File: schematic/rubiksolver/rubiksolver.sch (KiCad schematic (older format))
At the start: 14 parts, among them M1 Stepper_Motor_bipolar, M2 Stepper_Motor_bipolar, M3 Stepper_Motor_bipolar, M4 Stepper_Motor_bipolar

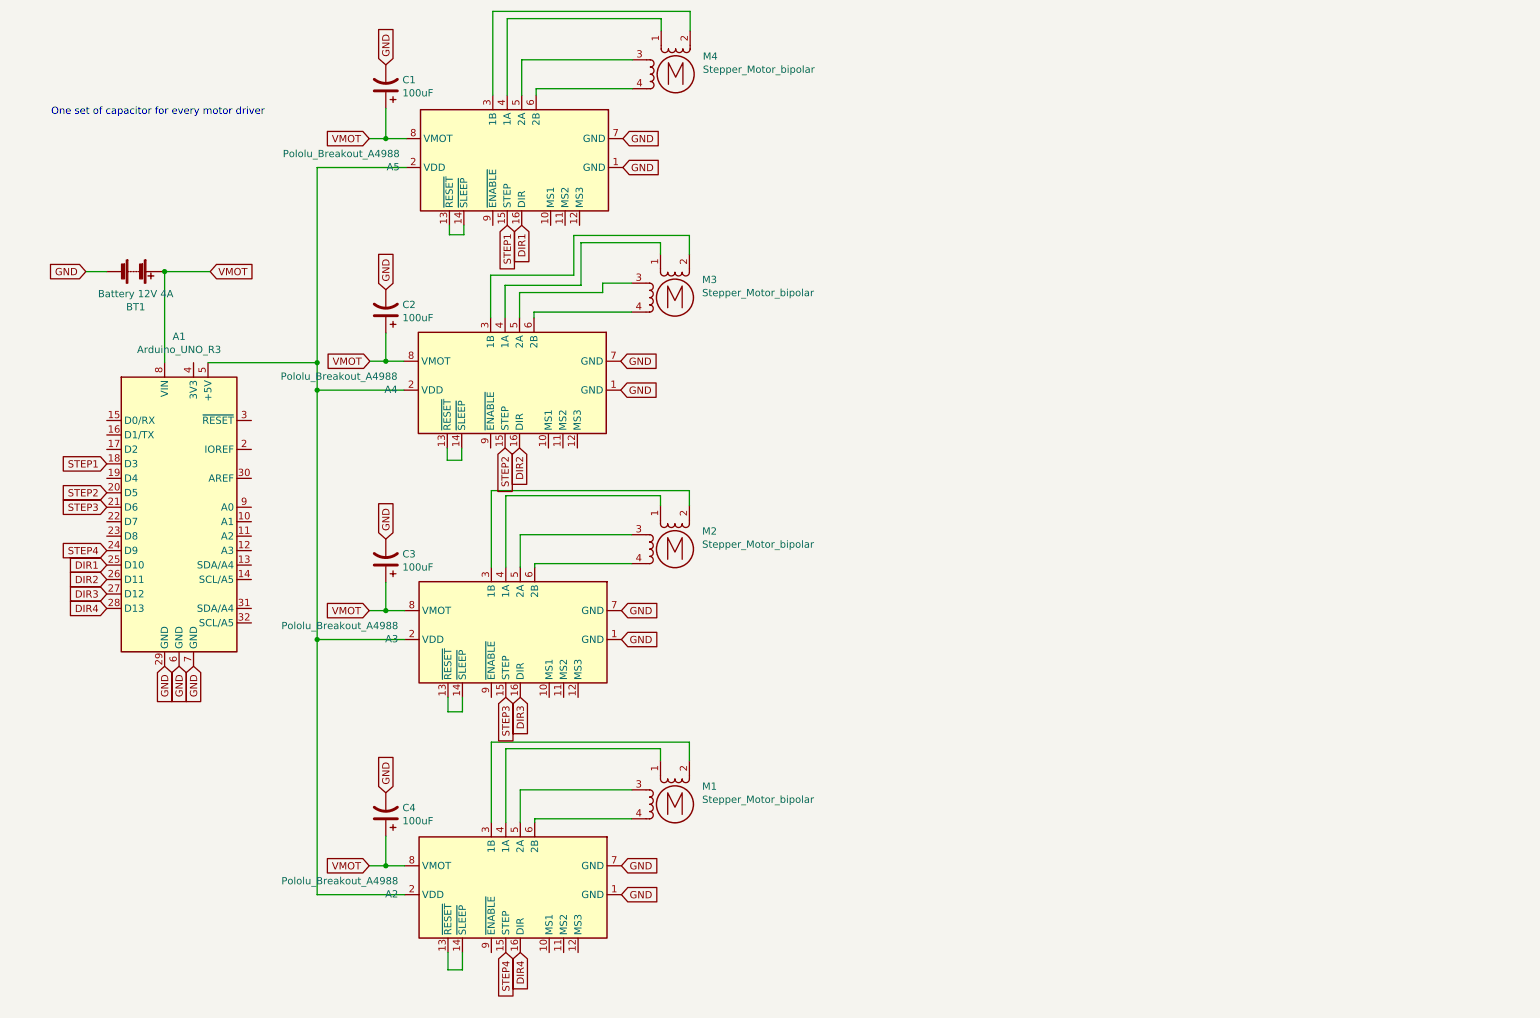
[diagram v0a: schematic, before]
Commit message: Changed models; updated schematic
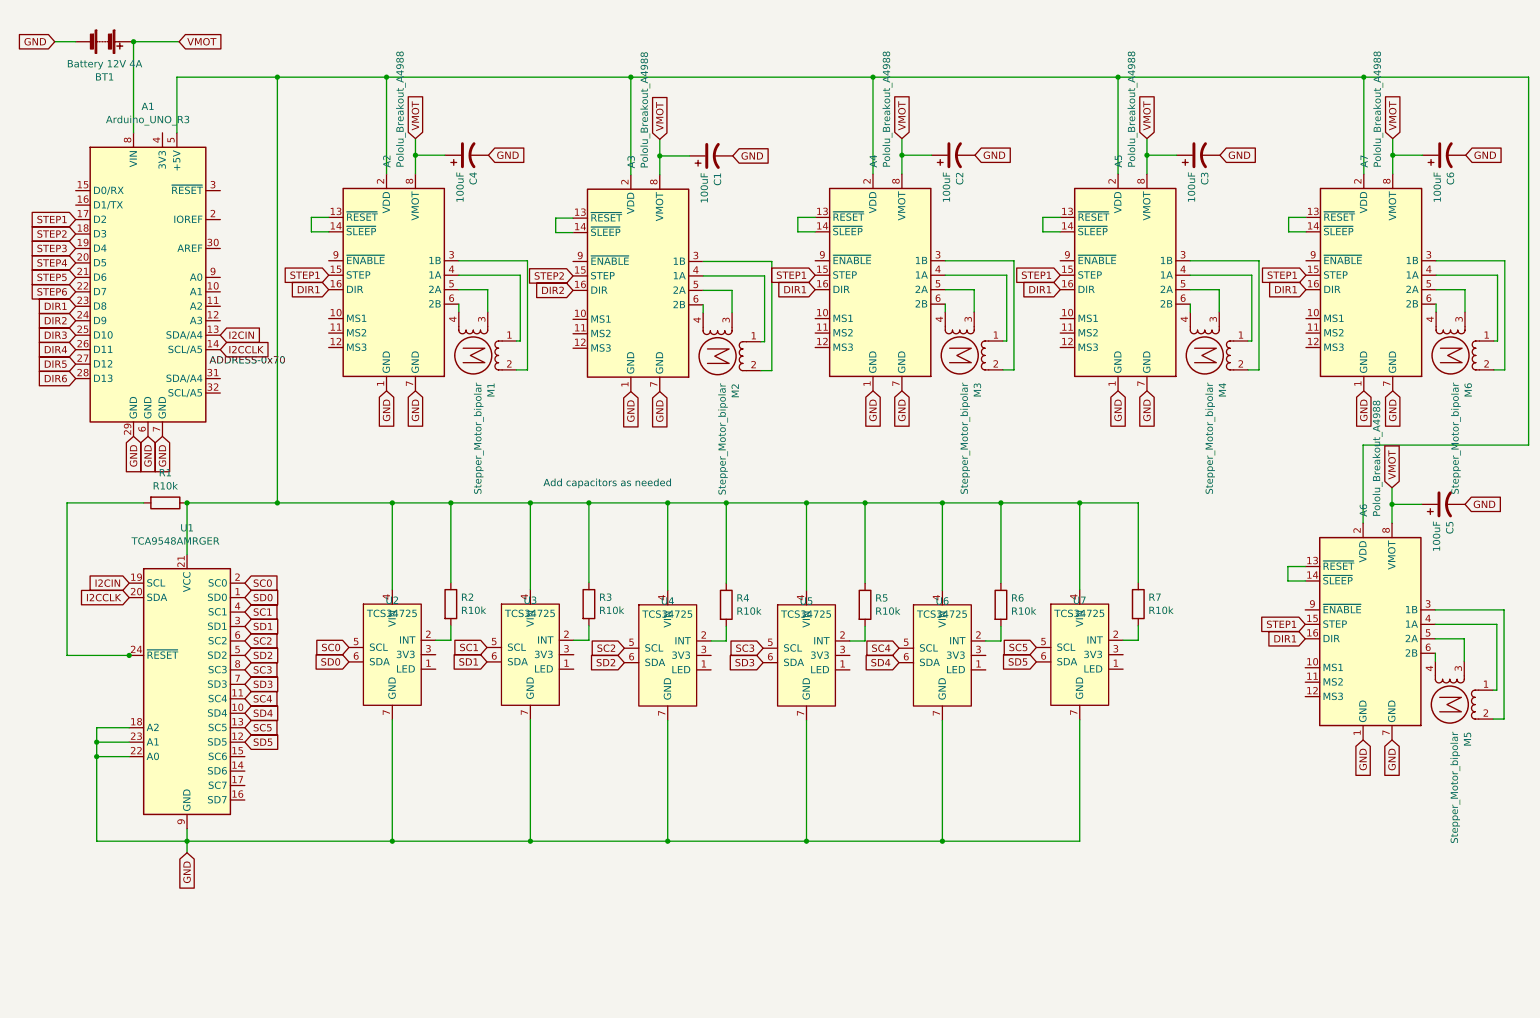
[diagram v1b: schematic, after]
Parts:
- added A6, A7: Pololu_Breakout_A4988, Module:Pololu_Breakout-16_15.2x20.3mm, symbol Driver_Motor:Pololu_Breakout_A4988
- added C5, C6: 100uF, symbol Device:CP1
- added M5, M6: Stepper_Motor_bipolar, symbol Motor:Stepper_Motor_bipolar
- added R1, R2, R3, R4, R5, R6, R7: R10k, symbol Device:R
- added U1: TCA9548AMRGER, Package_DFN_QFN:Texas_RGE0024C_EP2.1x2.1mm, symbol Interface_Expansion:TCA9548AMRGER
- added U2, U3, U4, U5, U6, U7: TCS34725, symbol TCS:TCS34725
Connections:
- net DIR1: now also A1.23 (D8), A2.16 (DIR), A4.16 (DIR), A6.16 (DIR), A7.16 (DIR); no longer A1.25 (D10)
- net DIR2: now also A1.24 (D9), A3.16 (DIR); no longer A1.26 (D11), A4.16 (DIR)
- net DIR3: now also A1.25 (D10); no longer A1.27 (D12), A3.16 (DIR)
- net DIR4: now also A1.26 (D11); no longer A1.28 (D13), A2.16 (DIR)
- net GND: now also A6.1 (GND), A6.7 (GND), A7.1 (GND), A7.7 (GND), C5.2, C6.2, U1.18 (A2), U1.22 (A0), U1.23 (A1), U1.9 (GND), U2.7 (GND), U3.7 (GND), U4.7 (GND), U5.7 (GND), U6.7 (GND), U7.7 (GND)
- net STEP1: now also A1.17 (D2), A2.15 (STEP), A4.15 (STEP), A6.15 (STEP), A7.15 (STEP); no longer A1.18 (D3)
- net STEP2: now also A1.18 (D3), A3.15 (STEP); no longer A1.20 (D5), A4.15 (STEP)
- net STEP3: now also A1.19 (D4); no longer A1.21 (D6), A3.15 (STEP)
- net STEP4: now also A1.20 (D5); no longer A1.24 (D9), A2.15 (STEP)
- net VMOT: now also A6.8 (VMOT), A7.8 (VMOT), C5.1, C6.1
- net at A1.5 (+5V), A2.2 (VDD), A3.2 (VDD)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: now also A6.2 (VDD), A7.2 (VDD), R1.1, R2.1, R3.1, R4.1, R5.1, R6.1, R7.1, U1.21 (VCC), U2.4 (VIN), U3.4 (VIN), U4.4 (VIN), U5.4 (VIN), U6.4 (VIN), U7.4 (VIN)
- net I2CIN: now reaches A1.13 (SDA/A4)
- net I2CIN: now also U1.19 (SCL)
- net I2CCLK: now reaches A1.14 (SCL/A5)
- net I2CCLK: now also U1.20 (SDA)
- net STEP6: now reaches A1.22 (D7)
- new net: R1.2, U1.24 (~RESET)
- new net: R2.2, U2.2 (INT)
- new net: A7.4 (1A), M6.1
- new net: A7.3 (1B), M6.2 (-)
- new net: A7.5 (2A), M6.3
- new net: A7.6 (2B), M6.4
- new net: A7.13 (~RESET), A7.14 (~SLEEP)
- new net: A6.4 (1A), M5.1
- new net: A6.3 (1B), M5.2 (-)
- new net: A6.5 (2A), M5.3
- new net: A6.6 (2B), M5.4
- new net: A6.13 (~RESET), A6.14 (~SLEEP)
- new net: R3.2, U3.2 (INT)
- new net: R4.2, U4.2 (INT)
- new net: R5.2, U5.2 (INT)
- new net: R6.2, U6.2 (INT)
- new net: R7.2, U7.2 (INT)
- new net DIR5: A1.27 (D12)
- new net DIR6: A1.28 (D13)
- new net SC0: U1.2 (SC0), U2.5 (SCL)
- new net SC1: U1.4 (SC1), U3.5 (SCL)
- new net SC2: U1.6 (SC2), U4.5 (SCL)
- new net SC3: U1.8 (SC3), U5.5 (SCL)
- new net SC4: U1.11 (SC4), U6.5 (SCL)
- new net SC5: U1.13 (SC5), U7.5 (SCL)
- new net SD0: U1.1 (SD0), U2.6 (SDA)
- new net SD1: U1.3 (SD1), U3.6 (SDA)
- new net SD2: U1.5 (SD2), U4.6 (SDA)
- new net SD3: U1.7 (SD3), U5.6 (SDA)
- new net SD4: U1.10 (SD4), U6.6 (SDA)
- new net SD5: U1.12 (SD5), U7.6 (SDA)
- new net STEP5: A1.21 (D6)
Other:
- note added: "Add capacitors as needed\n"
- note removed: "One set of capacitor for every motor driver\n"
- moved on the sheet: A1, A2, BT1, C4, M1

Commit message: Change schematic a bit
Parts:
- removed R2, R3, R4, R5, R6, R7: R10k, symbol Device:R
- U2, U3, U4, U5, U6, U7: symbol TCS:TCS34725 -> rubiksolver-rescue:TCS34725-TCS
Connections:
- net SC0: now also U1.6 (SC2); no longer U1.2 (SC0)
- net SC1: now also U1.8 (SC3); no longer U1.4 (SC1)
- net SC2: now also U1.11 (SC4); no longer U1.6 (SC2)
- net SC3: now also U1.13 (SC5); no longer U1.8 (SC3)
- net SC4: now also U1.15 (SC6); no longer U1.11 (SC4)
- net SC5: now also U1.17 (SC7); no longer U1.13 (SC5)
- net SD0: now also U1.5 (SD2); no longer U1.1 (SD0)
- net SD1: now also U1.7 (SD3); no longer U1.3 (SD1)
- net SD2: now also U1.10 (SD4); no longer U1.5 (SD2)
- net SD3: now also U1.12 (SD5); no longer U1.7 (SD3)
- net SD4: now also U1.14 (SD6); no longer U1.10 (SD4)
- net SD5: now also U1.16 (SD7); no longer U1.12 (SD5)
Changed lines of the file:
@@
 $EndComp
 $Comp
-L TCS:TCS34725 U2
+L rubiksolver-rescue:TCS34725-TCS U2
 U 1 1 5FDCE038
 P 3045 4550
@@
 Wire Wire Line
 	1000 6240 1000 5655
-Text GLabel 2025 4455 2    50   Input ~ 0
+Text GLabel 2025 4855 2    50   Input ~ 0
 SC0
-Text GLabel 2025 4555 2    50   Input ~ 0
+Text GLabel 2025 4955 2    50   Input ~ 0
 SD0
-Text GLabel 2025 4655 2    50   Input ~ 0
+Text GLabel 2025 5055 2    50   Input ~ 0
 SC1
-Text GLabel 2025 4755 2    50   Input ~ 0
+Text GLabel 2025 5155 2    50   Input ~ 0
 SD1
-Text GLabel 2025 4855 2    50   Input ~ 0
+Text GLabel 2025 5255 2    50   Input ~ 0
 SC2
-Text GLabel 2025 4955 2    50   Input ~ 0
+Text GLabel 2025 5355 2    50   Input ~ 0
 SD2
-Text GLabel 2025 5055 2    50   Input ~ 0
+Text GLabel 2025 5455 2    50   Input ~ 0
 SC3
-Text GLabel 2025 5155 2    50   Input ~ 0
+Text GLabel 2025 5555 2    50   Input ~ 0
 SD3
-Text GLabel 2025 5255 2    50   Input ~ 0
+Text GLabel 2025 5655 2    50   Input ~ 0
 SC4
-Text GLabel 2025 5355 2    50   Input ~ 0
+Text GLabel 2025 5755 2    50   Input ~ 0
 SD4
-Text GLabel 2025 5455 2    50   Input ~ 0
+Text GLabel 2025 5855 2    50   Input ~ 0
 SC5
-Text GLabel 2025 5555 2    50   Input ~ 0
+Text GLabel 2025 5955 2    50   Input ~ 0
 SD5
 Text GLabel 1455 3440 3    50   Input ~ 0
@@
 Wire Wire Line
 	3045 6240 3045 5400
-$Comp
-L Device:R R2
-U 1 1 5FF151B2
-P 3450 4600
-F 0 "R2" H 3520 4646 50  0000 L CNN
-F 1 "R10k" H 3520 4555 50  0000 L CNN
-F 2 "" V 3380 4600 50  0001 C CNN
-F 3 "~" H 3450 4600 50  0001 C CNN
-	1    3450 4600
-	1    0    0    -1
-$EndComp
-Wire Wire Line
-	3345 4850 3450 4850
-Wire Wire Line
-	3450 4850 3450 4750
-Wire Wire Line
-	3450 4450 3450 3900
-Wire Wire Line
-	3450 3900 3045 3900
 Connection ~ 3045 3900
 $Comp
-L TCS:TCS34725 U3
+L rubiksolver-rescue:TCS34725-TCS U3
 U 1 1 5FF2369D
 P 4000 4550
@@
 	4000 6240 4000 5400
 $Comp
-L Device:R R3
-U 1 1 5FF236A7
-P 4405 4600
-F 0 "R3" H 4475 4646 50  0000 L CNN
-F 1 "R10k" H 4475 4555 50  0000 L CNN
-F 2 "" V 4335 4600 50  0001 C CNN
-F 3 "~" H 4405 4600 50  0001 C CNN
-	1    4405 4600
-	1    0    0    -1
-$EndComp
-Wire Wire Line
-	4300 4850 4405 4850
-Wire Wire Line
-	4405 4850 4405 4750
-$Comp
-L TCS:TCS34725 U4
+L rubiksolver-rescue:TCS34725-TCS U4
 U 1 1 5FF2B39B
 P 4950 4555
@@
 SD2
 $Comp
-L Device:R R4
-U 1 1 5FF2B3A5
-P 5355 4605
-F 0 "R4" H 5425 4651 50  0000 L CNN
-F 1 "R10k" H 5425 4560 50  0000 L CNN
-F 2 "" V 5285 4605 50  0001 C CNN
-F 3 "~" H 5355 4605 50  0001 C CNN
-	1    5355 4605
-	1    0    0    -1
-$EndComp
-Wire Wire Line
-	5250 4855 5355 4855
-Wire Wire Line
-	5355 4855 5355 4755
-$Comp
-L TCS:TCS34725 U5
+L rubiksolver-rescue:TCS34725-TCS U5
 U 1 1 5FF33485
 P 5910 4555
@@
 	1    0    0    -1
 $EndComp
+Text GLabel 5610 5005 0    50   Input ~ 0
+SD3
+Text GLabel 6550 5005 0    50   Input ~ 0
+SD4
+$Comp
+L rubiksolver-rescue:TCS34725-TCS U7
+U 1 1 5FF42F52
+P 7800 4550
+F 0 "U7" H 7800 4525 50  0000 C CNN
+F 1 "TCS34725" H 7800 4434 50  0000 C CNN
+F 2 "" H 7800 4550 50  0001 C CNN
+F 3 "" H 7800 4550 50  0001 C CNN
+	1    7800 4550
+	1    0    0    -1
+$EndComp
+Text GLabel 7500 5000 0    50   Input ~ 0
+SD5
+Wire Wire Line
+	7800 3900 7800 4500
+Wire Wire Line
+	7800 6240 7800 5400
+Wire Wire Line
+	4950 3900 4950 4505
+Connection ~ 4000 3900
+Wire Wire Line
+	5910 3900 5910 4505
+Connection ~ 4950 3900
+Wire Wire Line
+	6850 3900 6850 4505
+Connection ~ 5910 3900
+Connection ~ 6850 3900
+Connection ~ 3045 6240
+Wire Wire Line
+	4950 5405 4950 6240
+Wire Wire Line
+	3045 6240 4000 6240
+Connection ~ 4000 6240
+Wire Wire Line
+	4000 6240 4950 6240
+Wire Wire Line
+	4950 6240 5910 6240
+Wire Wire Line
+	5910 6240 5910 5405
+Connection ~ 4950 6240
+Wire Wire Line
+	6850 5405 6850 6240
+Wire Wire Line
+	6850 6240 5910 6240
+Connection ~ 5910 6240
+Wire Wire Line
+	6850 6240 7800 6240
+Connection ~ 6850 6240
+Text Notes 4090 3800 0    50   ~ 0
+Add capacitors as needed\n
+Wire Wire Line
+	3045 3900 4000 3900
+Wire Wire Line
+	4000 3900 4950 3900
 Text GLabel 5610 4905 0    50   Input ~ 0
 SC3
-Text GLabel 5610 5005 0    50   Input ~ 0
-SD3
-$Comp
-L Device:R R5
-U 1 1 5FF3348F
-P 6315 4605
-F 0 "R5" H 6385 4651 50  0000 L CNN
-F 1 "R10k" H 6385 4560 50  0000 L CNN
-F 2 "" V 6245 4605 50  0001 C CNN
-F 3 "~" H 6315 4605 50  0001 C CNN
-	1    6315 4605
-	1    0    0    -1
-$EndComp
-Wire Wire Line
-	6210 4855 6315 4855
-Wire Wire Line
-	6315 4855 6315 4755
-$Comp
-L TCS:TCS34725 U6
+Wire Wire Line
+	4950 3900 5910 3900
+Wire Wire Line
+	5910 3900 6850 3900
+Text GLabel 6550 4905 0    50   Input ~ 0
+SC4
+$Comp
+L rubiksolver-rescue:TCS34725-TCS U6
 U 1 1 5FF3AED2
 P 6850 4555
@@
 	1    0    0    -1
 $EndComp
-Text GLabel 6550 4905 0    50   Input ~ 0
-SC4
-Text GLabel 6550 5005 0    50   Input ~ 0
-SD4
-$Comp
-L Device:R R6
-U 1 1 5FF3AEDC
-P 7255 4605
-F 0 "R6" H 7325 4651 50  0000 L CNN
-F 1 "R10k" H 7325 4560 50  0000 L CNN
-F 2 "" V 7185 4605 50  0001 C CNN
-F 3 "~" H 7255 4605 50  0001 C CNN
-	1    7255 4605
-	1    0    0    -1
-$EndComp
-Wire Wire Line
-	7150 4855 7255 4855
-Wire Wire Line
-	7255 4855 7255 4755
-$Comp
-L TCS:TCS34725 U7
-U 1 1 5FF42F52
-P 7800 4550
-F 0 "U7" H 7800 4525 50  0000 C CNN
-F 1 "TCS34725" H 7800 4434 50  0000 C CNN
-F 2 "" H 7800 4550 50  0001 C CNN
-F 3 "" H 7800 4550 50  0001 C CNN
-	1    7800 4550
-	1    0    0    -1
-$EndComp
+Wire Wire Line
+	6850 3900 7800 3900
 Text GLabel 7500 4900 0    50   Input ~ 0
 SC5
-Text GLabel 7500 5000 0    50   Input ~ 0
-SD5
-Wire Wire Line
-	7800 3900 7800 4500
-Wire Wire Line
-	7800 6240 7800 5400
-$Comp
-L Device:R R7
-U 1 1 5FF42F5C
-P 8205 4600
-F 0 "R7" H 8275 4646 50  0000 L CNN
-F 1 "R10k" H 8275 4555 50  0000 L CNN
-F 2 "" V 8135 4600 50  0001 C CNN
-F 3 "~" H 8205 4600 50  0001 C CNN
-	1    8205 4600
-	1    0    0    -1
-$EndComp
-Wire Wire Line
-	8100 4850 8205 4850
-Wire Wire Line
-	8205 4850 8205 4750
-Wire Wire Line
-	3450 3900 4000 3900
-Connection ~ 3450 3900
-Wire Wire Line
-	4000 3900 4405 3900
-Wire Wire Line
-	4950 3900 4950 4505
-Connection ~ 4000 3900
-Wire Wire Line
-	4950 3900 5355 3900
-Wire Wire Line
-	5910 3900 5910 4505
-Connection ~ 4950 3900
-Wire Wire Line
-	5910 3900 6315 3900
-Wire Wire Line
-	6850 3900 6850 4505
-Connection ~ 5910 3900
-Wire Wire Line
-	6850 3900 7255 3900
-Connection ~ 6850 3900
-Connection ~ 3045 6240
-Wire Wire Line
-	4950 5405 4950 6240
-Wire Wire Line
-	3045 6240 4000 6240
-Connection ~ 4000 6240
-Wire Wire Line
-	4000 6240 4950 6240
-Wire Wire Line
-	4950 6240 5910 6240
-Wire Wire Line
-	5910 6240 5910 5405
-Connection ~ 4950 6240
-Wire Wire Line
-	6850 5405 6850 6240
-Wire Wire Line
-	6850 6240 5910 6240
-Connection ~ 5910 6240
-Wire Wire Line
-	6850 6240 7800 6240
-Connection ~ 6850 6240
-Wire Wire Line
-	4405 4450 4405 3900
-Connection ~ 4405 3900
-Wire Wire Line
-	4405 3900 4950 3900
-Wire Wire Line
-	5355 4455 5355 3900
-Connection ~ 5355 3900
-Wire Wire Line
-	5355 3900 5910 3900
-Wire Wire Line
-	6315 4455 6315 3900
-Connection ~ 6315 3900
-Wire Wire Line
-	6315 3900 6850 3900
-Connection ~ 7255 3900
-Wire Wire Line
-	7255 3900 7800 3900
-Wire Wire Line
-	7255 3900 7255 4455
-Wire Wire Line
-	8205 4450 8205 3900
-Wire Wire Line
-	8205 3900 7800 3900
-Connection ~ 7800 3900
-Text Notes 4090 3800 0    50   ~ 0
-Add capacitors as needed\n
 $EndSCHEMATC

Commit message: Removed a receiver
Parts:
- removed R1: R10k, symbol Device:R
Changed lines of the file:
@@
 Wire Wire Line
 	1230 4955 1225 4955
-Wire Wire Line
-	795  4955 795  3900
-Connection ~ 1225 4955
-Wire Wire Line
-	1225 4955 795  4955
-Wire Wire Line
-	795  3900 1325 3900
-$Comp
-L Device:R R1
-U 1 1 5FEAE06C
-P 1475 3900
-F 0 "R1" V 1268 3900 50  0000 C CNN
-F 1 "R10k" V 1359 3900 50  0000 C CNN
-F 2 "" V 1405 3900 50  0001 C CNN
-F 3 "~" H 1475 3900 50  0001 C CNN
-	1    1475 3900
-	0    1    1    0
-$EndComp
-Connection ~ 1625 3900
 Text GLabel 1225 4455 0    50   Input ~ 0
 I2CIN
